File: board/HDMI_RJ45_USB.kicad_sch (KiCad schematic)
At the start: 19 parts, among them J1 RJ45, T1 H5007NL, U1 HDMI/USB, U11 TPD4EUSB30, U12 RT9742GGJ5, U5 RT9742GGJ5, U6 TPD4EUSB30

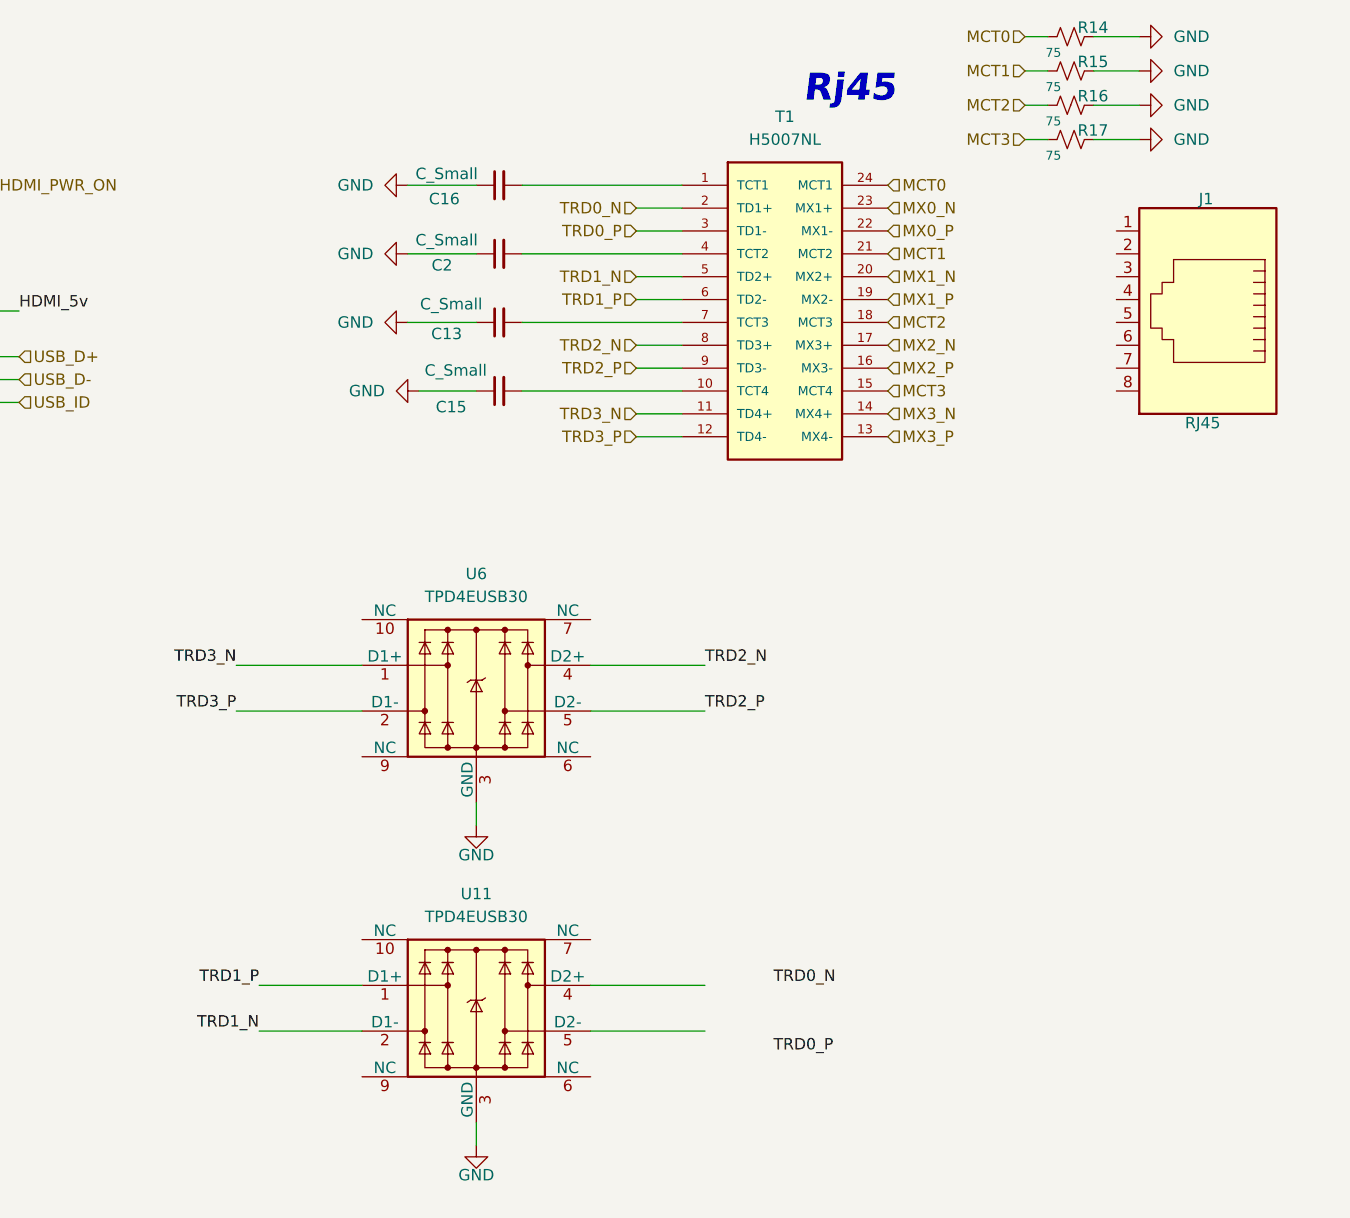
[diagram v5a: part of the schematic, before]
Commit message: got the ethernet routed
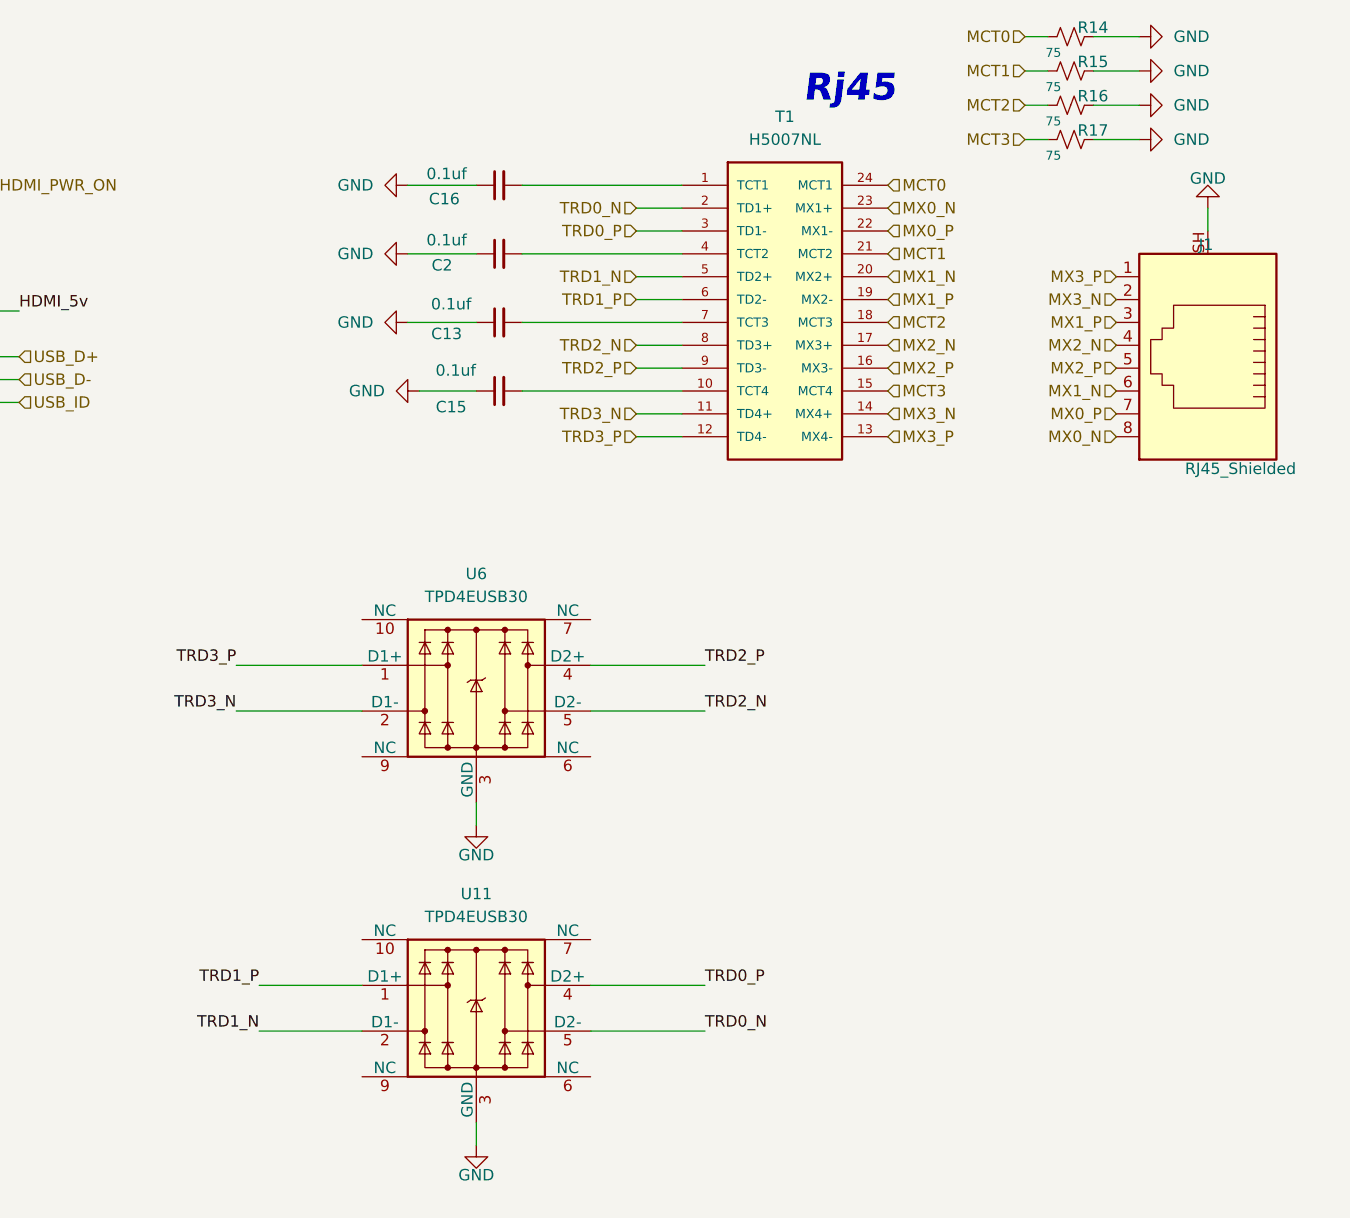
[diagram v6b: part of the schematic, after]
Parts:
- C13, C15, C16, C2: value C_Small -> 0.1uf
- J1: value RJ45 -> RJ45_Shielded; symbol Connector:RJ45 -> Connector:RJ45_Shielded; now in the parts list
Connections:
- net GND: now also J1.SH
- net MX0_N: now also J1.8
- net MX0_P: now also J1.7
- net MX1_N: now also J1.6
- net MX1_P: now also J1.3
- net MX2_N: now also J1.4
- net MX2_P: now also J1.5
- net MX3_N: now also J1.2
- net MX3_P: now also J1.1
- net TRD0_N: now also U11.5 (D2-)
- net TRD0_P: now also U11.4 (D2+)
- net TRD2_N: now also U6.5 (D2-); no longer U6.4 (D2+)
- net TRD2_P: now also U6.4 (D2+); no longer U6.5 (D2-)
- net TRD3_N: now also U6.2 (D1-); no longer U6.1 (D1+)
- net TRD3_P: now also U6.1 (D1+); no longer U6.2 (D1-)
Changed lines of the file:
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@@
 	(wire
 		(pts
+			(xy 260.35 39.37) (xy 260.35 36.83)
+		)
+		(stroke
+			(width 0)
+			(type default)
+		)
+	)
+	(wire
+		(pts
 			(xy 154.94 128.27) (xy 166.37 128.27)
 		)
@@
 		)
 	)
-	(label "TRD3_P"
-		(at 152.4 92.71 180)
+	(label "TRD0_P"
+		(at 204.47 123.19 0)
 		(effects
 			(font
 				(size 1.27 1.27)
 			)
-			(justify right bottom)
+			(justify left bottom)
 		)
 	)
@@
 		)
 	)
-	(label "TRD2_N"
-		(at 204.47 87.63 0)
+	(label "TRD0_N"
+		(at 204.47 128.27 0)
 		(effects
 			(font
@@
 		)
 	)
-	(label "TRD0_P"
-		(at 212.09 130.81 0)
+	(label "TRD3_N"
+		(at 152.4 92.71 180)
 		(effects
 			(font
 				(size 1.27 1.27)
 			)
-			(justify left bottom)
+			(justify right bottom)
 		)
 	)
-	(label "HDMI_5v"
-		(at 128.27 48.26 0)
+	(label "TRD2_N"
+		(at 204.47 92.71 0)
 		(effects
 			(font
@@
 		)
 	)
-	(label "TRD0_N"
-		(at 212.09 123.19 0)
+	(label "HDMI_5v"
+		(at 128.27 48.26 0)
 		(effects
 			(font
@@
 		)
 	)
-	(label "TRD3_N"
+	(label "TRD3_P"
 		(at 152.4 87.63 180)
 		(effects
@@
 	)
 	(label "TRD2_P"
-		(at 204.47 92.71 0)
+		(at 204.47 87.63 0)
 		(effects
 			(font
@@
 		)
 	)
+	(hierarchical_label "MX0_P"
+		(shape input)
+		(at 250.19 59.69 180)
+		(effects
+			(font
+				(size 1.27 1.27)
+			)
+			(justify right)
+		)
+	)
 	(hierarchical_label "SD_DAT0"
 		(shape input)
@@
 		)
 	)
+	(hierarchical_label "MX3_N"
+		(shape input)
+		(at 250.19 46.99 180)
+		(effects
+			(font
+				(size 1.27 1.27)
+			)
+			(justify right)
+		)
+	)
 	(hierarchical_label "MX3_P"
 		(shape input)
@@
 		)
 	)
+	(hierarchical_label "MX2_N"
+		(shape input)
+		(at 250.19 52.07 180)
+		(effects
+			(font
+				(size 1.27 1.27)
+			)
+			(justify right)
+		)
+	)
 	(hierarchical_label "USB_D-"
 		(shape input)
@@
 		)
 	)
+	(hierarchical_label "MX1_P"
+		(shape input)
+		(at 250.19 49.53 180)
+		(effects
+			(font
+				(size 1.27 1.27)
+			)
+			(justify right)
+		)
+	)
 	(hierarchical_label "SD_DAT2"
 		(shape input)
@@
 		)
 	)
+	(hierarchical_label "MX0_N"
+		(shape input)
+		(at 250.19 62.23 180)
+		(effects
+			(font
+				(size 1.27 1.27)
+			)
+			(justify right)
+		)
+	)
 	(hierarchical_label "TRD3_P"
 		(shape input)
@@
 		)
 	)
+	(hierarchical_label "MX2_P"
+		(shape input)
+		(at 250.19 54.61 180)
+		(effects
+			(font
+				(size 1.27 1.27)
+			)
+			(justify right)
+		)
+	)
 	(hierarchical_label "MCT0"
 		(shape input)
@@
 		)
 	)
+	(hierarchical_label "MX1_N"
+		(shape input)
+		(at 250.19 57.15 180)
+		(effects
+			(font
+				(size 1.27 1.27)
+			)
+			(justify right)
+		)
+	)
 	(hierarchical_label "MX2_P"
 		(shape input)
@@
 		)
 	)
+	(hierarchical_label "MX3_P"
+		(shape input)
+		(at 250.19 44.45 180)
+		(effects
+			(font
+				(size 1.27 1.27)
+			)
+			(justify right)
+		)
+	)
 	(hierarchical_label "USB_ID"
 		(shape input)
@@
 			)
 		)
-		(property "Value" "C_Small"
+		(property "Value" "0.1uf"
 			(at 176.276 47.498 90)
 			(effects
@@
 	)
 	(symbol
+		(lib_id "power:GND")
+		(at 260.35 36.83 180)
+		(unit 1)
+		(exclude_from_sim no)
+		(in_bom yes)
+		(on_board yes)
+		(dnp no)
+		(property "Reference" "#PWR015"
+			(at 260.35 30.48 0)
+			(effects
+				(font
+					(size 1.27 1.27)
+				)
+				(hide yes)
+			)
+		)
+		(property "Value" "GND"
+			(at 260.35 33.528 0)
+			(effects
+				(font
+					(size 1.27 1.27)
+				)
+			)
+		)
+		(property "Footprint" ""
+			(at 260.35 36.83 0)
+			(effects
+				(font
+					(size 1.27 1.27)
+				)
+				(hide yes)
+			)
+		)
+		(property "Datasheet" ""
+			(at 260.35 36.83 0)
+			(effects
+				(font
+					(size 1.27 1.27)
+				)
+				(hide yes)
+			)
+		)
+		(property "Description" "Power symbol creates a global label with name \"GND\" , ground"
+			(at 260.35 36.83 0)
+			(effects
+				(font
+					(size 1.27 1.27)
+				)
+				(hide yes)
+			)
+		)
+		(pin "1"
+		)
+		(instances
+			(project "apple_pi_tv_board"
+				(path "/391fcf0b-b604-4ad0-921e-8f3dad9a49eb/c5e1f0e2-c40e-4ccf-aeb8-8ca027446308"
+					(reference "#PWR015")
+					(unit 1)
+				)
+			)
+		)
+	)
+	(symbol
 		(lib_id "Power_Protection:TPD4EUSB30")
 		(at 179.07 125.73 0)
@@
 	)
 	(symbol
-		(lib_id "Connector:RJ45")
-		(at 260.35 46.99 180)
+		(lib_id "Connector:RJ45_Shielded")
+		(at 260.35 52.07 180)
 		(unit 1)
 		(exclude_from_sim no)
-		(in_bom no)
+		(in_bom yes)
 		(on_board yes)
 		(dnp no)
 		(property "Reference" "J1"
-			(at 259.334 35.814 0)
+			(at 259.334 40.894 0)
 			(effects
 				(font
@@
 			)
 		)
-		(property "Value" "RJ45"
-			(at 257.81 60.706 0)
+		(property "Value" "RJ45_Shielded"
+			(at 257.81 65.786 0)
 			(effects
 				(font
@@
 		)
 		(property "Footprint" "apple_tv_parts:apple_tv_ethernet"
-			(at 260.35 47.625 90)
+			(at 260.35 52.705 90)
 			(effects
 				(font
@@
 		)
 		(property "Datasheet" "~"
-			(at 260.35 47.625 90)
+			(at 260.35 52.705 90)
 			(effects
 				(font
@@
 			)
 		)
-		(property "Description" "RJ connector, 8P8C (8 positions 8 connected)"
-			(at 260.35 46.99 0)
+		(property "Description" "RJ connector, 8P8C (8 positions 8 connected), Shielded"
+			(at 260.35 52.07 0)
 			(effects
 				(font
@@
 		(pin "3"
 		)
+		(pin "SH"
+		)
 		(instances
 			(project "apple_pi_tv_board"
@@
 			)
 		)
-		(property "Value" "C_Small"
+		(property "Value" "0.1uf"
 			(at 176.784 54.864 90)
 			(effects
@@
 			)
 		)
-		(property "Value" "C_Small"
+		(property "Value" "0.1uf"
 			(at 175.768 33.02 90)
 			(effects
@@
 			)
 		)
-		(property "Value" "C_Small"
+		(property "Value" "0.1uf"
 			(at 175.768 40.386 90)
 			(effects
